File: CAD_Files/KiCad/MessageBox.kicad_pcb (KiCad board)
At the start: 2 copper layers, 39.5 x 31 mm, 9 parts, among them J1 Conn_01x03_Female, J2 1.8 TFT, J3 Reed Switch, Q1 2N7002, U1 WeMos_D1_mini

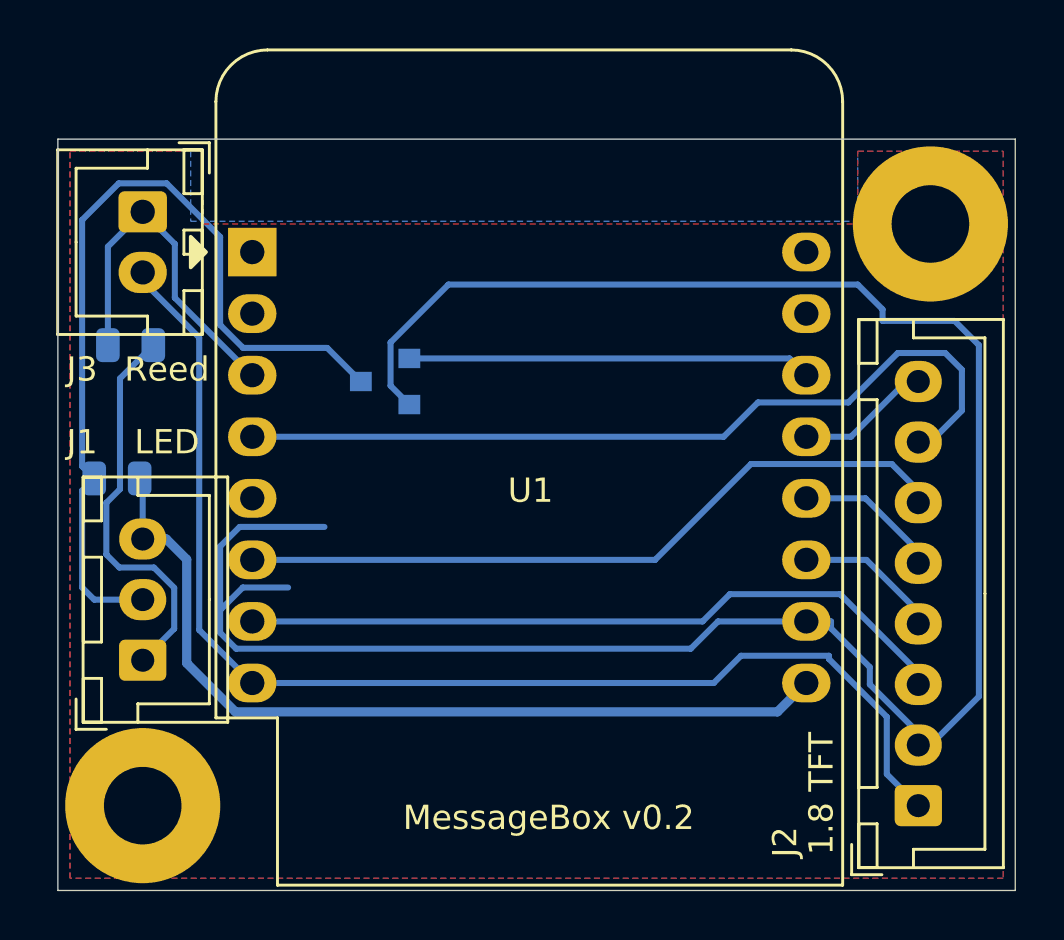
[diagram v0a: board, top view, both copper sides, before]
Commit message: Updated board, fixes for build, added debug logic
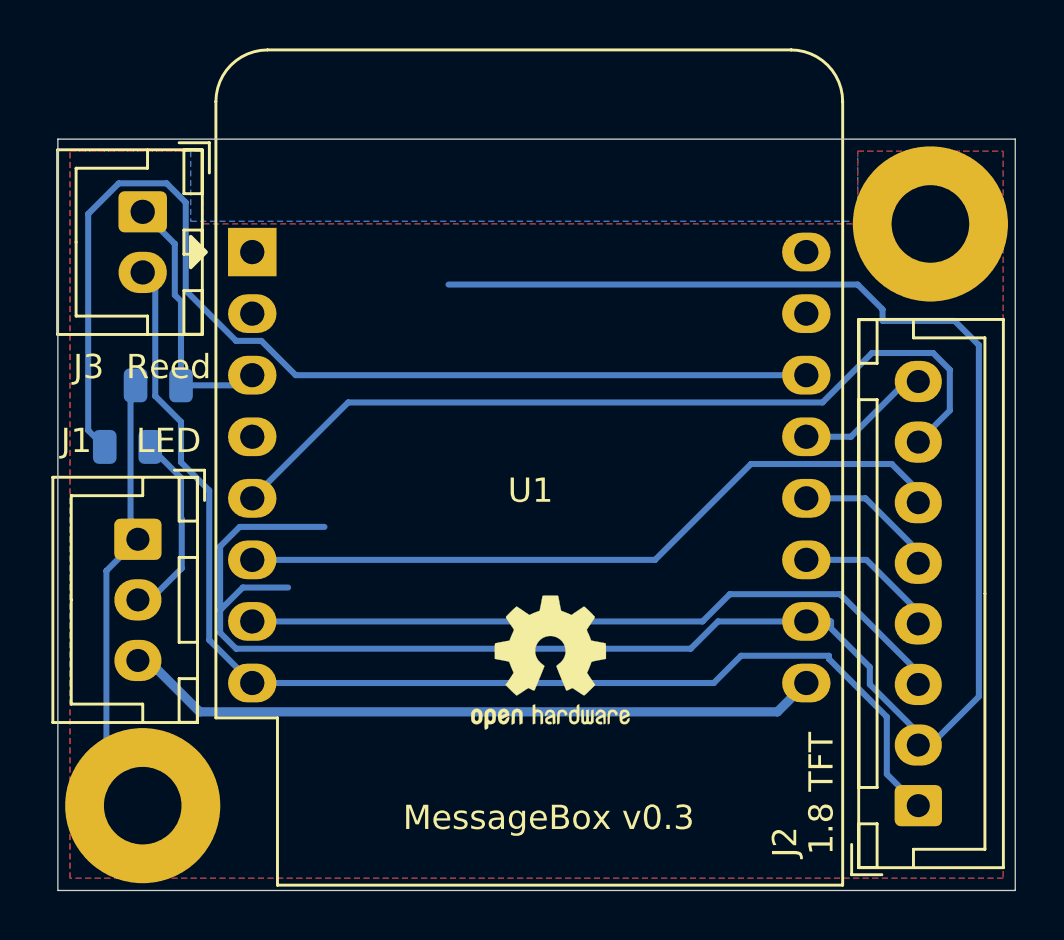
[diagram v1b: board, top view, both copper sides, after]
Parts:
- removed Q1: 2N7002, Package_TO_SOT_SMD:SOT-23
- added REF**: OSHW-Logo2_7.3x6mm_SilkScreen, Symbol:OSHW-Logo2_7.3x6mm_SilkScreen, F.Cu at (172.3, 90.6)
- moved J1 4.99 mm to (155.3, 85.5), turned to 270 degrees
- moved R2 2.02 mm to (156.1, 79.2), turned to 0 degrees
- moved R1 1.37 mm to (154.9, 81.7), turned to 180 degrees
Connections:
- J1 pad 3: Net-(J1-Pad3) -> +5V
- R1 pad 2: Net-(J1-Pad3) -> Net-(R1-Pad2)
- U1 pad 14: Net-(Q1-Pad1) -> Net-(R1-Pad2)
- U1 pad 4: Net-(J2-Pad7) -> Net-(U1-Pad4)
- U1 pad 5: Net-(U1-Pad5) -> Net-(J2-Pad7)
- U1 pad 9: Net-(J1-Pad3) -> +5V
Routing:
- net Net-(R1-Pad2): track 0.00 -> 45.5 mm
- net Net-(J1-Pad3): track 35.9 -> 0.00 mm
- net Net-(J1-Pad2): track 35.9 -> 7.39 mm
- net +5V: track 0.00 -> 28.5 mm
- net Net-(Q1-Pad1): track 16.7 -> 0.00 mm
- net Net-(J3-Pad1): track 14.7 -> 10.9 mm
- net GND: track 108.0 -> 104.3 mm
- net Net-(J2-Pad7): track 34.5 -> 35.1 mm
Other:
- board text added: "MessageBox v0.3"
- board text removed: "MessageBox v0.2"
